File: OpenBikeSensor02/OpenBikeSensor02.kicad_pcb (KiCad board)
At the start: 2 copper layers, 58.2 x 62.2 mm, 34 parts, among them J1 Conn_01x02_Male, J10 Conn_02x03_Odd_Even, J11 Conn_01x02_Male, J2 Conn_01x04_Female, J3 Conn_01x04_Male, J4 Conn_01x04_Male, J5 Conn_01x05_Male, J6 Conn_01x02_Male, J7 Conn_01x06_Male, J8 Conn_01x06_Male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

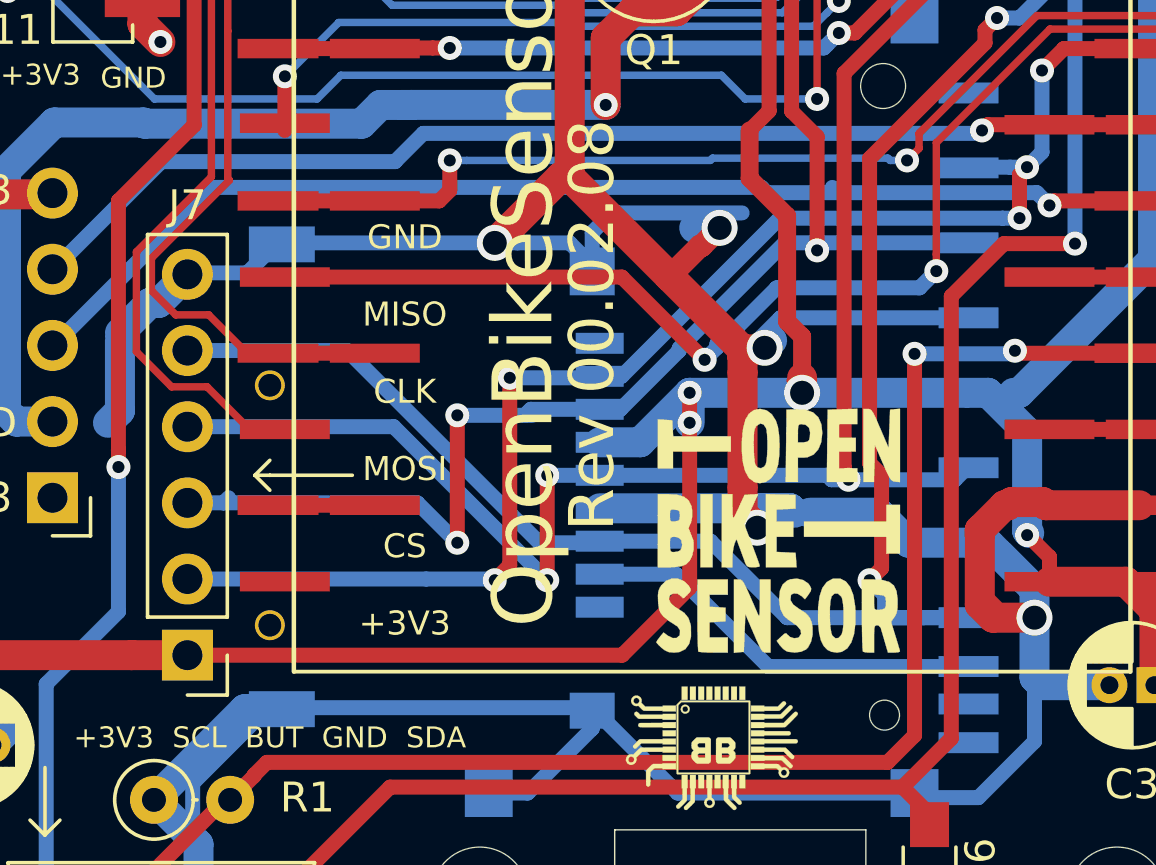
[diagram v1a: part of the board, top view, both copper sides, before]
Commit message: fixed wiring of the Micro SD slot
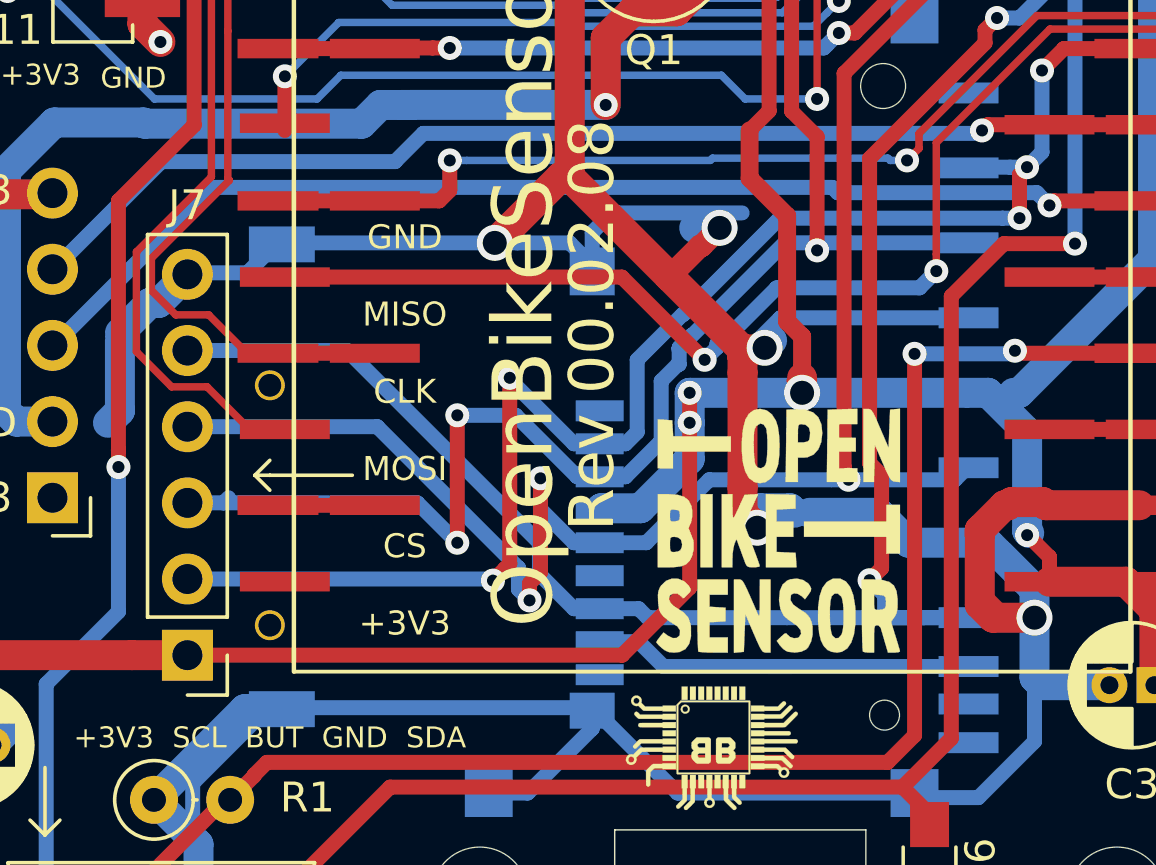
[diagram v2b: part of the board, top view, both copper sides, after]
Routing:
- net GND: track 263.7 -> 257.3 mm
- net SD_CMD: track 68.0 -> 71.6 mm
- net SD_CLK: track 57.0 -> 60.3 mm
- net SD_CD: track 47.2 -> 50.5 mm
- net +3V3: track 236.2 -> 237.4 mm
- net SD_DAT0: track 63.0 -> 63.6 mm

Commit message: increased Rev to 00.02.09 generated new Gerber
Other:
- board text added: "Rev 00.02.09"
- board text removed: "Rev 00.02.08"
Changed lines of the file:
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@@
   )
   (setup
-    (last_trace_width 0.5)
+    (last_trace_width 0.25)
     (user_trace_width 0.2)
     (user_trace_width 0.5)
@@
       (drillshape 0)
       (scaleselection 1)
-      (outputdirectory "Gerber/"))
+      (outputdirectory "../GerberJLC/"))
   )
   (net 0 "")
@@
     (effects (font (size 1 1) (thickness 0.15)) (justify mirror))
   )
-  (gr_text "Rev 00.02.08" (at 65.786 88.773 90) (layer B.SilkS)
+  (gr_text "Rev 00.02.09" (at 65.786 88.773 90) (layer B.SilkS)
     (effects (font (size 1.5 1.5) (thickness 0.2)) (justify mirror))
   )
-  (gr_text "Rev 00.02.08\n" (at 47.498 86.741 90) (layer F.SilkS)
+  (gr_text "Rev 00.02.09\n" (at 47.498 86.741 90) (layer F.SilkS)
     (effects (font (size 1.5 1.5) (thickness 0.2)))
   )
